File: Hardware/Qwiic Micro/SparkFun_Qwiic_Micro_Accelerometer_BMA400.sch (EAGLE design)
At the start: 30 parts, among them J1 QWIIC_RIGHT_ANGLE, U1 BMA400

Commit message: Update version number to v10
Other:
- note added: "v10"
- note removed: "v01"
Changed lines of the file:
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@@
 <plain>
 <text x="167.64" y="10.16" size="2.54" layer="94" font="vector">Dryw Wade</text>
-<text x="238.76" y="7.62" size="2.54" layer="94" font="vector">v01</text>
+<text x="238.76" y="7.62" size="2.54" layer="94" font="vector">v10</text>
 <text x="73.66" y="180.34" size="2.54" layer="94" font="vector" align="center">Accelerometer - BMA400</text>
 <text x="38.1" y="76.2" size="2.54" layer="94" font="vector" align="center">Connectors</text>

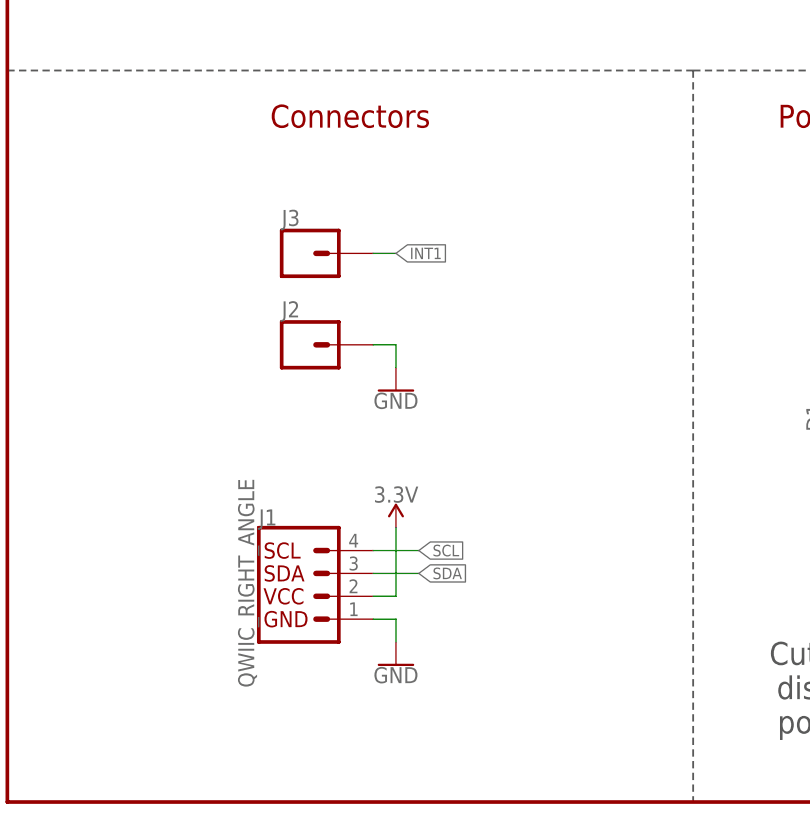
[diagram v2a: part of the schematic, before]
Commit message: Add text about 22AWG wires to Micro schematic
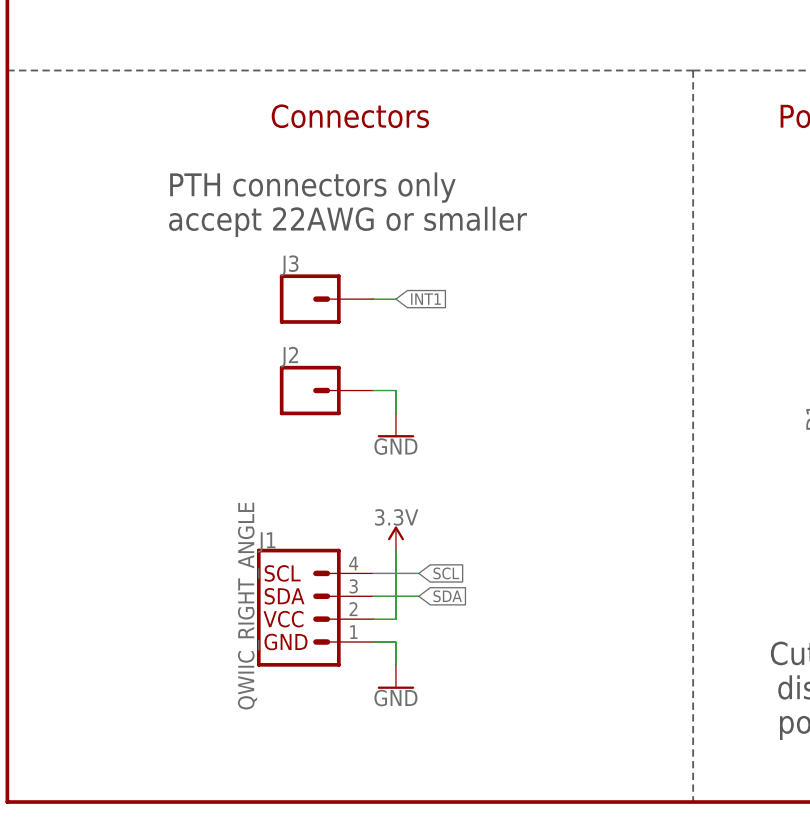
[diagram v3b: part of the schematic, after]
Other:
- note added: "PTH connectors only accept 22AWG or smaller"
- moved on the sheet: J1, J2, J3
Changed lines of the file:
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@@
 VDD: 1.72V - 3.6V
 VDDIO: 1.2V - 3.6V</text>
+<text x="17.78" y="63.5" size="2.54" layer="97" font="vector">PTH connectors only
+accept 22AWG or smaller</text>
 </plain>
 <instances>
@@
 </instance>
 <instance part="LOGO1" gate="G$1" x="180.34" y="40.64" smashed="yes"/>
-<instance part="J1" gate="G$1" x="33.02" y="22.86" smashed="yes">
-<attribute name="VALUE" x="25.654" y="12.7" size="1.778" layer="96" font="vector" rot="R90" align="top-left"/>
-<attribute name="NAME" x="27.94" y="30.734" size="1.778" layer="95" font="vector"/>
-</instance>
-<instance part="GND1" gate="1" x="43.18" y="15.24" smashed="yes">
-<attribute name="VALUE" x="43.18" y="14.986" size="1.778" layer="96" align="top-center"/>
-</instance>
-<instance part="SUPPLY1" gate="G$1" x="43.18" y="30.48" smashed="yes">
-<attribute name="VALUE" x="43.18" y="33.274" size="1.778" layer="96" align="bottom-center"/>
+<instance part="J1" gate="G$1" x="33.02" y="20.32" smashed="yes">
+<attribute name="VALUE" x="25.654" y="10.16" size="1.778" layer="96" font="vector" rot="R90" align="top-left"/>
+<attribute name="NAME" x="27.94" y="28.194" size="1.778" layer="95" font="vector"/>
+</instance>
+<instance part="GND1" gate="1" x="43.18" y="12.7" smashed="yes">
+<attribute name="VALUE" x="43.18" y="12.446" size="1.778" layer="96" align="top-center"/>
+</instance>
+<instance part="SUPPLY1" gate="G$1" x="43.18" y="27.94" smashed="yes">
+<attribute name="VALUE" x="43.18" y="30.734" size="1.778" layer="96" align="bottom-center"/>
 </instance>
 <instance part="LOGO2" gate="G$1" x="190.5" y="33.02" smashed="yes"/>
@@
 <attribute name="VALUE" x="129.54" y="66.294" size="1.778" layer="96" align="bottom-center"/>
 </instance>
-<instance part="J2" gate="G$1" x="33.02" y="50.8" smashed="yes">
-<attribute name="VALUE" x="30.48" y="45.974" size="1.778" layer="96" font="vector"/>
-<attribute name="NAME" x="30.48" y="53.848" size="1.778" layer="95" font="vector"/>
-</instance>
-<instance part="J3" gate="G$1" x="33.02" y="60.96" smashed="yes">
-<attribute name="VALUE" x="30.48" y="56.134" size="1.778" layer="96" font="vector"/>
-<attribute name="NAME" x="30.48" y="64.008" size="1.778" layer="95" font="vector"/>
+<instance part="J2" gate="G$1" x="33.02" y="45.72" smashed="yes">
+<attribute name="VALUE" x="30.48" y="40.894" size="1.778" layer="96" font="vector"/>
+<attribute name="NAME" x="30.48" y="48.768" size="1.778" layer="95" font="vector"/>
+</instance>
+<instance part="J3" gate="G$1" x="33.02" y="55.88" smashed="yes">
+<attribute name="VALUE" x="30.48" y="51.054" size="1.778" layer="96" font="vector"/>
+<attribute name="NAME" x="30.48" y="58.928" size="1.778" layer="95" font="vector"/>
 </instance>
 <instance part="TP1" gate="G$1" x="129.54" y="12.7" smashed="yes">
@@
 </instance>
 <instance part="LOGO4" gate="G$1" x="223.52" y="44.958" smashed="yes"/>
-<instance part="GND2" gate="1" x="43.18" y="45.72" smashed="yes">
-<attribute name="VALUE" x="43.18" y="45.466" size="1.778" layer="96" align="top-center"/>
+<instance part="GND2" gate="1" x="43.18" y="40.64" smashed="yes">
+<attribute name="VALUE" x="43.18" y="40.386" size="1.778" layer="96" align="top-center"/>
 </instance>
 <instance part="ADR" gate="G$1" x="205.74" y="101.6" smashed="yes" rot="MR0">
@@
 <segment>
 <pinref part="GND1" gate="1" pin="GND"/>
-<wire x1="43.18" y1="17.78" x2="43.18" y2="20.32" width="0.1524" layer="91"/>
+<wire x1="43.18" y1="15.24" x2="43.18" y2="17.78" width="0.1524" layer="91"/>
 <pinref part="J1" gate="G$1" pin="1"/>
-<wire x1="43.18" y1="20.32" x2="40.64" y2="20.32" width="0.1524" layer="91"/>
+<wire x1="43.18" y1="17.78" x2="40.64" y2="17.78" width="0.1524" layer="91"/>
 </segment>
 <segment>
@@
 <segment>
 <pinref part="GND2" gate="1" pin="GND"/>
-<wire x1="43.18" y1="48.26" x2="43.18" y2="50.8" width="0.1524" layer="91"/>
-<wire x1="43.18" y1="50.8" x2="40.64" y2="50.8" width="0.1524" layer="91"/>
+<wire x1="43.18" y1="43.18" x2="43.18" y2="45.72" width="0.1524" layer="91"/>
+<wire x1="43.18" y1="45.72" x2="40.64" y2="45.72" width="0.1524" layer="91"/>
 <pinref part="J2" gate="G$1" pin="1"/>
 </segment>
@@
 <segment>
 <pinref part="SUPPLY1" gate="G$1" pin="3.3V"/>
-<wire x1="43.18" y1="30.48" x2="43.18" y2="22.86" width="0.1524" layer="91"/>
+<wire x1="43.18" y1="27.94" x2="43.18" y2="20.32" width="0.1524" layer="91"/>
 <pinref part="J1" gate="G$1" pin="2"/>
-<wire x1="43.18" y1="22.86" x2="40.64" y2="22.86" width="0.1524" layer="91"/>
+<wire x1="43.18" y1="20.32" x2="40.64" y2="20.32" width="0.1524" layer="91"/>
 </segment>
 <segment>
@@
 <segment>
 <pinref part="J1" gate="G$1" pin="4"/>
-<wire x1="40.64" y1="27.94" x2="45.72" y2="27.94" width="0.1524" layer="91"/>
-<label x="45.72" y="27.94" size="1.27" layer="95" font="vector" xref="yes"/>
+<wire x1="40.64" y1="25.4" x2="45.72" y2="25.4" width="0.1524" layer="91"/>
+<label x="45.72" y="25.4" size="1.27" layer="95" font="vector" xref="yes"/>
 </segment>
 <segment>
@@
 <segment>
 <pinref part="J1" gate="G$1" pin="3"/>
-<wire x1="40.64" y1="25.4" x2="45.72" y2="25.4" width="0.1524" layer="91"/>
-<label x="45.72" y="25.4" size="1.27" layer="95" font="vector" xref="yes"/>
+<wire x1="40.64" y1="22.86" x2="45.72" y2="22.86" width="0.1524" layer="91"/>
+<label x="45.72" y="22.86" size="1.27" layer="95" font="vector" xref="yes"/>
 </segment>
 <segment>
@@
 </segment>
 <segment>
-<wire x1="40.64" y1="60.96" x2="43.18" y2="60.96" width="0.1524" layer="91"/>
-<label x="43.18" y="60.96" size="1.27" layer="95" font="vector" xref="yes"/>
+<wire x1="40.64" y1="55.88" x2="43.18" y2="55.88" width="0.1524" layer="91"/>
+<label x="43.18" y="55.88" size="1.27" layer="95" font="vector" xref="yes"/>
 <pinref part="J3" gate="G$1" pin="1"/>
 </segment>

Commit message: Remove library file
Part is in SFE Eagle library, update part in design
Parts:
- U1: device BMA400:BMA400 -> SparkFun-Sensors:BMA400
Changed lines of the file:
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@@
 <parts>
 <part name="FRAME1" library="SparkFun-Aesthetics" deviceset="FRAME-LETTER" device=""/>
-<part name="U1" library="BMA400" deviceset="BMA400" device=""/>
+<part name="U1" library="SparkFun-Sensors" deviceset="BMA400" device=""/>
 <part name="LOGO1" library="SparkFun-Aesthetics" deviceset="QWIIC_LOGO" device="_3MM" value="QWIIC_LOGO_3MM"/>
 <part name="J1" library="SparkFun-Connectors" deviceset="QWIIC_CONNECTOR" device="JS-1MM" value="QWIIC_RIGHT_ANGLE"/>
